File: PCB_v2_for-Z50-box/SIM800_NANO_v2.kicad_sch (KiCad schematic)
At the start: 42 parts, among them J1 PJ-002BH, J2 TB002-500-02BE, J3 Screw_Terminal_1x3, J4 Screw_Terminal_1x3, K1 SANYOU_SRD_Form_C, K2 SANYOU_SRD_Form_C, Q1 MMBT5551L, Q2 MMBT5551L, SW1 SIM800_RST, U1 LM2596S-ADJ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

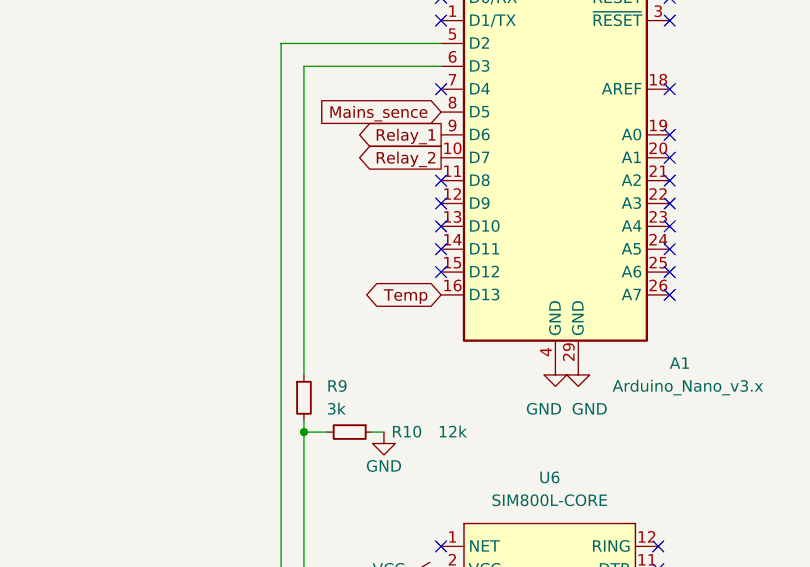
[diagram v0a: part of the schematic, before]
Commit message: Temp sensor pin13 to pin12
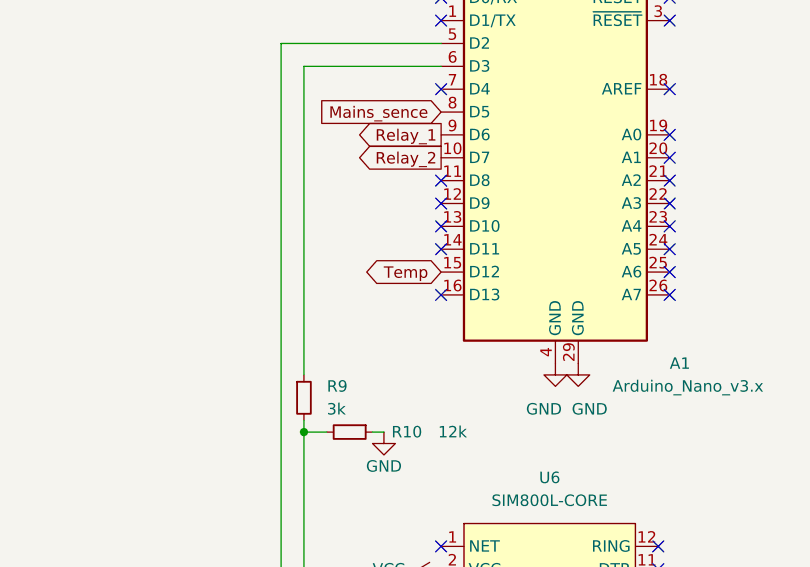
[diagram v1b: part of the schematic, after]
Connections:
- net Temp: now also A1.15 (D12); no longer A1.16 (D13)
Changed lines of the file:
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@@
   (no_connect (at 100.965 114.935))
   (no_connect (at 126.365 104.775))
-  (no_connect (at 100.965 117.475))
+  (no_connect (at 100.965 120.015))
   (no_connect (at 100.965 107.315))
   (no_connect (at 125.095 160.655))
@@
     )
   )
-  (global_label "Temp" (shape bidirectional) (at 100.965 120.015 180) (fields_autoplaced)
-    (effects (font (size 1.27 1.27)) (justify right))
-    (property "Intersheet References" "${INTERSHEET_REFS}" (id 0) (at 93.6533 119.9356 0)
-      (effects (font (size 1.27 1.27)) (justify right) hide)
-    )
+  (global_label "Temp" (shape bidirectional) (at 100.965 117.475 180) (fields_autoplaced)
+    (effects (font (size 1.27 1.27)) (justify right))
+    (property "Intersheet References" "${INTERSHEET_REFS}" (id 0) (at 93.6533 117.3956 0)
+      (effects (font (size 1.27 1.27)) (justify right) hide)
+    )
